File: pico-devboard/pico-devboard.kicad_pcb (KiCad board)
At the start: 2 copper layers, 113.4 x 132.1 mm, 10 parts, among them J1 Power Header, J2 GPIO Header, J3 Off-board Header, J4 Pico Dev, J5 Pico Dev Programming, SW1 SW_Push_Dual, SW2 SW_SPDT, U1 Pico

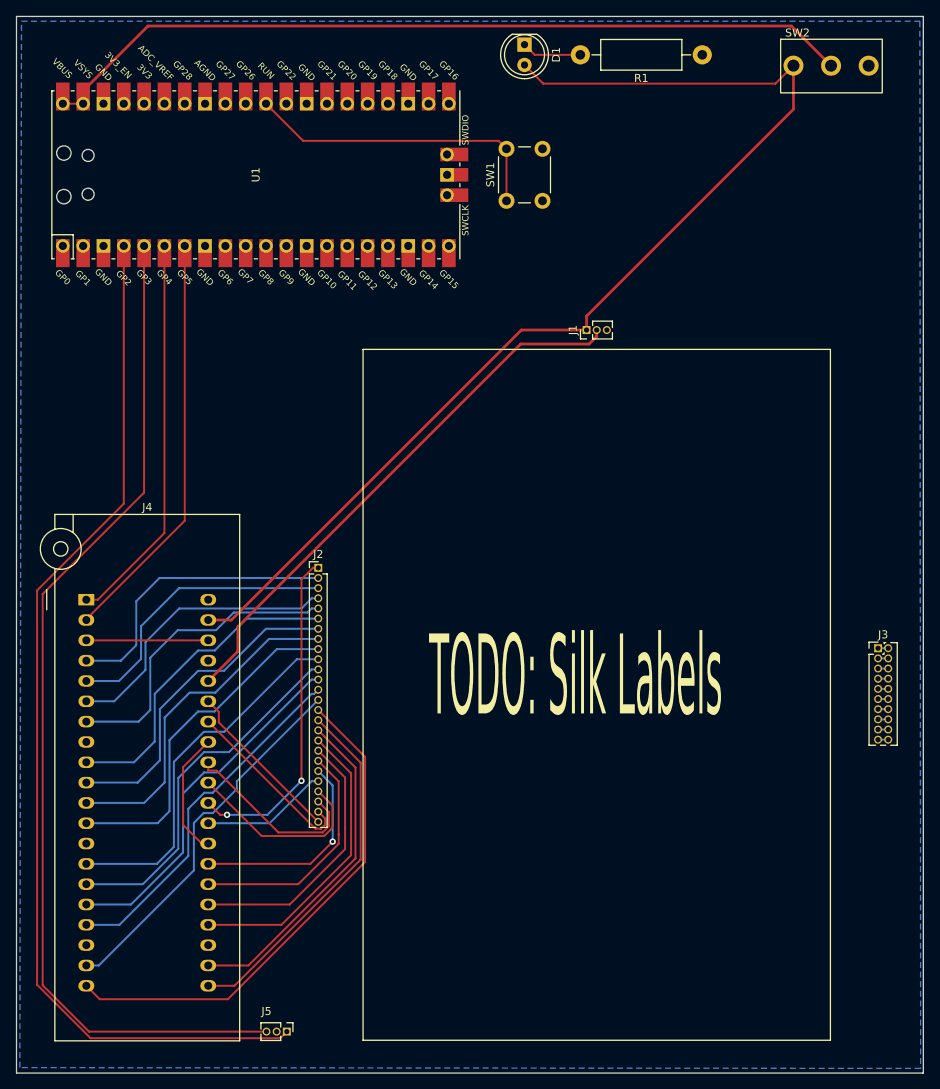
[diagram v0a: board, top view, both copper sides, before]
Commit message: Silkscreen, small adjustments, readme updates
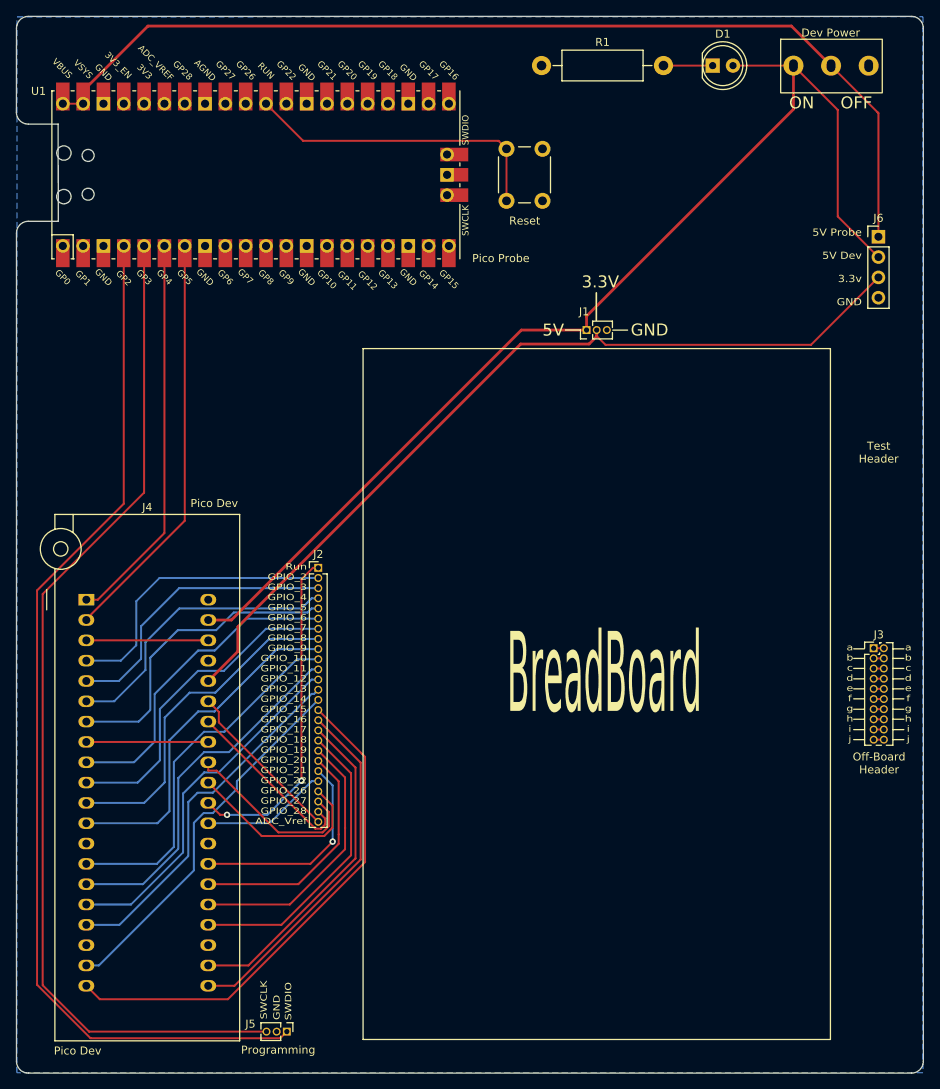
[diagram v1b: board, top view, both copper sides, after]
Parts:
- added J6: Test Header, Connector_PinHeader_2.54mm:PinHeader_1x04_P2.54mm_Vertical, F.Cu at (138.2, 52.9)
- Dev Power: renamed from SW2
- moved D1 23.7 mm to (117.5, 31.6), turned to 0 degrees
- moved R1 20.1 mm to (96.1, 31.5), turned to 0 degrees
- moved J3 0.55 mm to (137.6, 104.4)
- renumbered SW1 to Reset
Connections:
- D1 pad 2: +5V -> /5V_switched
- Dev Power pad 1: +5V -> /5V_switched
- Dev Power pad 2: Net-(U1-Pad39) -> +5V
- J1 pad 1: +5V -> /5V_switched
- J4 pad 39: +5V -> /5V_switched
- U1 pad 39: Net-(U1-Pad39) -> +5V
- U1 pad 40: Net-(U1-Pad39) -> +5V
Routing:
- net /5V_switched: track 0.00 -> 142.0 mm
- net Net-(U1-Pad39): track 103.0 -> 0.00 mm
- net +3V3: track 69.0 -> 108.9 mm
- net +5V: track 141.6 -> 126.9 mm
- net Net-(D1-Pad1): track 7.51 -> 6.15 mm
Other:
- outline, holes or cut-outs redrawn
- board text added: "3.3V"
- board text added: "5V"
- board text added: "5V Probe 5V Dev 3.3v GND"
- board text added: "BreadBoard"
- board text added: "GND"
- board text added: "ON OFF"
- board text added: "Off-Board Header"
- board text added: "Pico Dev"
- board text added: "Pico Probe"
- board text added: "Programming"
- board text added: "Run GPIO_2 GPIO_3 GPIO_4 GPIO_5 GPIO_6 GPIO_7 GPIO_8 GPIO_9 GPIO_10 GPIO_11 GPIO_12 GPIO_13 GPIO_14 GPIO_15 GPIO_16 GPIO_17 GPIO_18 GPIO_19 GPIO_20 GPIO_21 GPIO_22 GPIO_26 GPIO_27 GPIO_28 ADC_Vref"
- board text added: "SWCLK"
- board text added: "SWDIO"
- board text added: "Test Header"
- board text added: "a b c d e f g h i j"
- board text removed: "TODO: Silk Labels"

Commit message: Fixing header spacing issue and re-routing
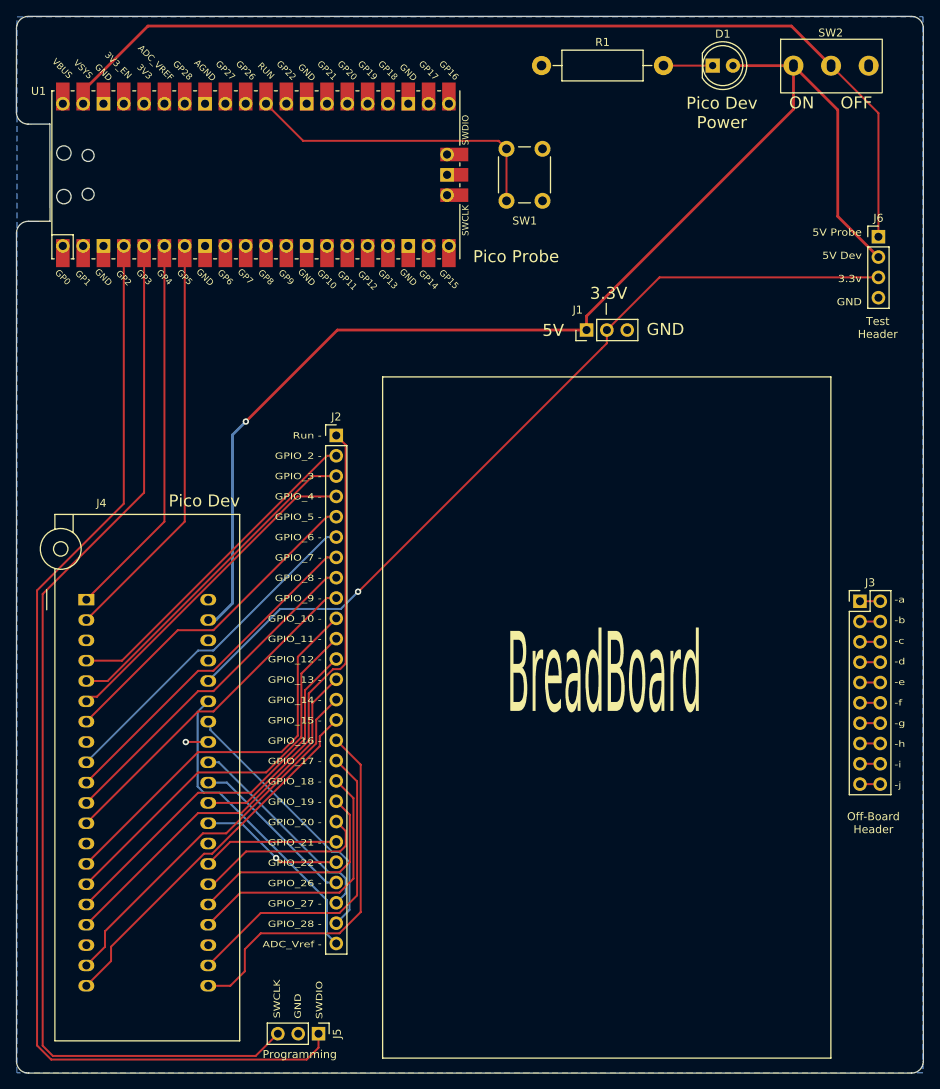
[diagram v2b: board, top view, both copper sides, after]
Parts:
- J1, J5: footprint Connector_PinHeader_1.27mm:PinHeader_1x03_P1.27mm_Vertical -> Connector_PinHeader_2.54mm:PinHeader_1x03_P2.54mm_Vertical
- J2: footprint Connector_PinHeader_1.27mm:PinHeader_1x26_P1.27mm_Vertical -> Connector_PinHeader_2.54mm:PinHeader_1x26_P2.54mm_Vertical
- J3: footprint Connector_PinHeader_1.27mm:PinHeader_2x10_P1.27mm_Vertical -> Connector_PinHeader_2.54mm:PinHeader_2x10_P2.54mm_Vertical
- SW2: renamed from Dev Power
- moved J2 16.7 mm to (70.5, 77.8)
- moved J3 6.12 mm to (135.9, 98.5)
- moved J5 3.97 mm to (68.2, 152.6)
- renumbered Reset to SW1
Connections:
- SW2 pad 3: GND -> unconnected-(SW2-Pad3)
- U1 pad 40: +5V -> unconnected-(U1-Pad40)
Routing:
- net GND: track 31.7 -> 2.81 mm, vias 0 -> 1
- net /ADC_VREF: track 20.8 -> 39.2 mm
- net /GPIO_15: track 64.1 -> 46.8 mm
- net /RUN: track 42.3 -> 56.8 mm, vias 2 -> 0
- net /5V_switched: track 142.0 -> 154.3 mm, vias 0 -> 1
- net /SWDIO: track 131.2 -> 142.7 mm
- net /GPIO_28: track 22.3 -> 33.7 mm
- net /GPIO_21: track 26.3 -> 17.1 mm, vias 1 -> 0
- net /SWCLK: track 128.0 -> 136.3 mm
- net /GPIO_20: track 29.8 -> 22.7 mm
- net /GPIO_3: track 36.2 -> 41.9 mm
- net /GPIO_4: track 36.4 -> 41.9 mm
- net /GPIO_19: track 33.7 -> 28.2 mm
- net /GPIO_2: track 36.5 -> 41.9 mm
- net /GPIO_10: track 45.8 -> 49.7 mm
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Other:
- outline, holes or cut-outs redrawn
- board text added: "-a -b -c -d -e -f -g -h -i -j"
- board text added: "Pico Dev Power"
- board text added: "Run - GPIO_2 - GPIO_3 - GPIO_4 - GPIO_5 - GPIO_6 - GPIO_7 - GPIO_8 - GPIO_9 - GPIO_10 - GPIO_11 - GPIO_12 - GPIO_13 - GPIO_14 - GPIO_15 - GPIO_16 - GPIO_17 - GPIO_18 - GPIO_19 - GPIO_20 - GPIO_21 - GPIO_22 - GPIO_26 - GPIO_27 - GPIO_28 - ADC_Vref -"
- board text removed: "Pico Dev"
- board text removed: "Run GPIO_2 GPIO_3 GPIO_4 GPIO_5 GPIO_6 GPIO_7 GPIO_8 GPIO_9 GPIO_10 GPIO_11 GPIO_12 GPIO_13 GPIO_14 GPIO_15 GPIO_16 GPIO_17 GPIO_18 GPIO_19 GPIO_20 GPIO_21 GPIO_22 GPIO_26 GPIO_27 GPIO_28 ADC_Vref"
- board text removed: "a b c d e f g h i j"

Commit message: v1.0.0 fab files
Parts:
- added REF**: OSHW-Logo2_9.8x8mm_SilkScreen, Symbol:OSHW-Logo2_9.8x8mm_SilkScreen, F.Cu at (137.8, 152.0)
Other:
- board text added: "JLCJLCJLCJLC"
- board text added: "v1.0.0"
